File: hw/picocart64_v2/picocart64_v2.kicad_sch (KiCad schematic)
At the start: 0 parts

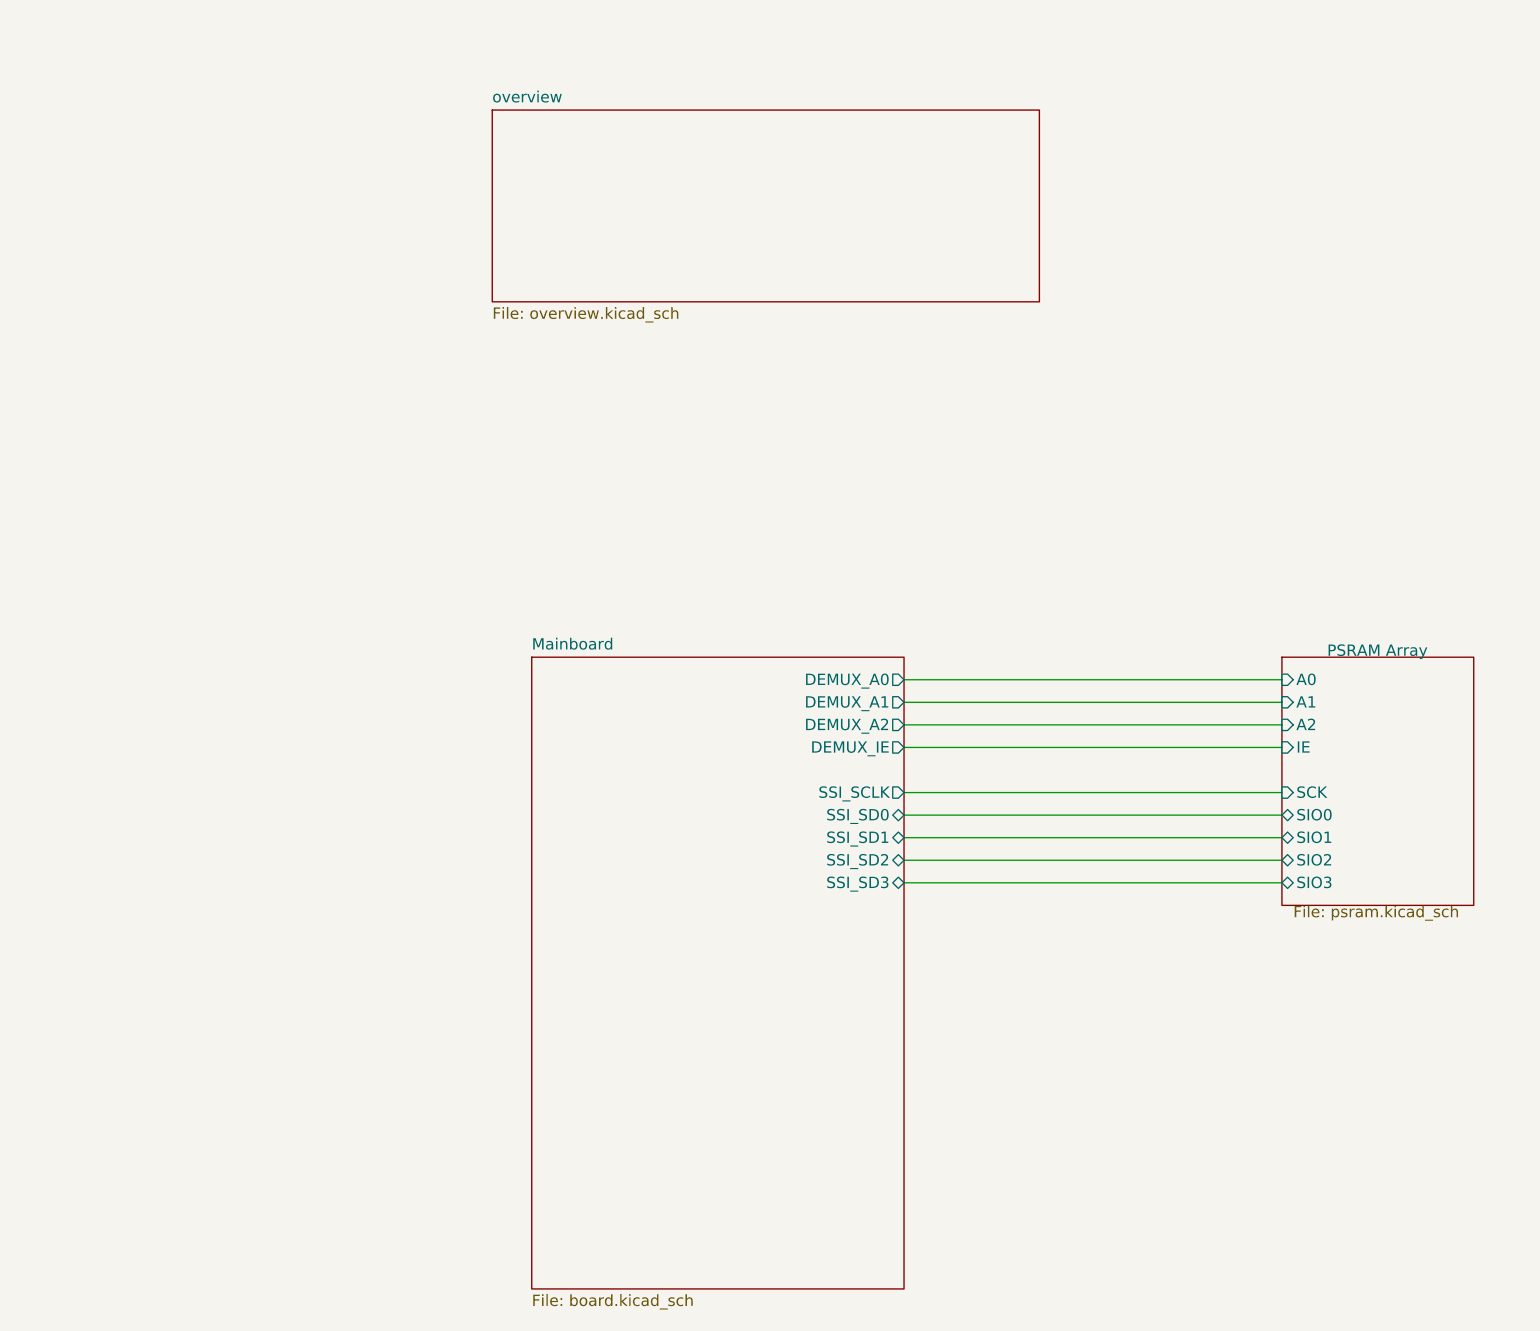
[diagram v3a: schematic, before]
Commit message: Documented and figured out some stuff
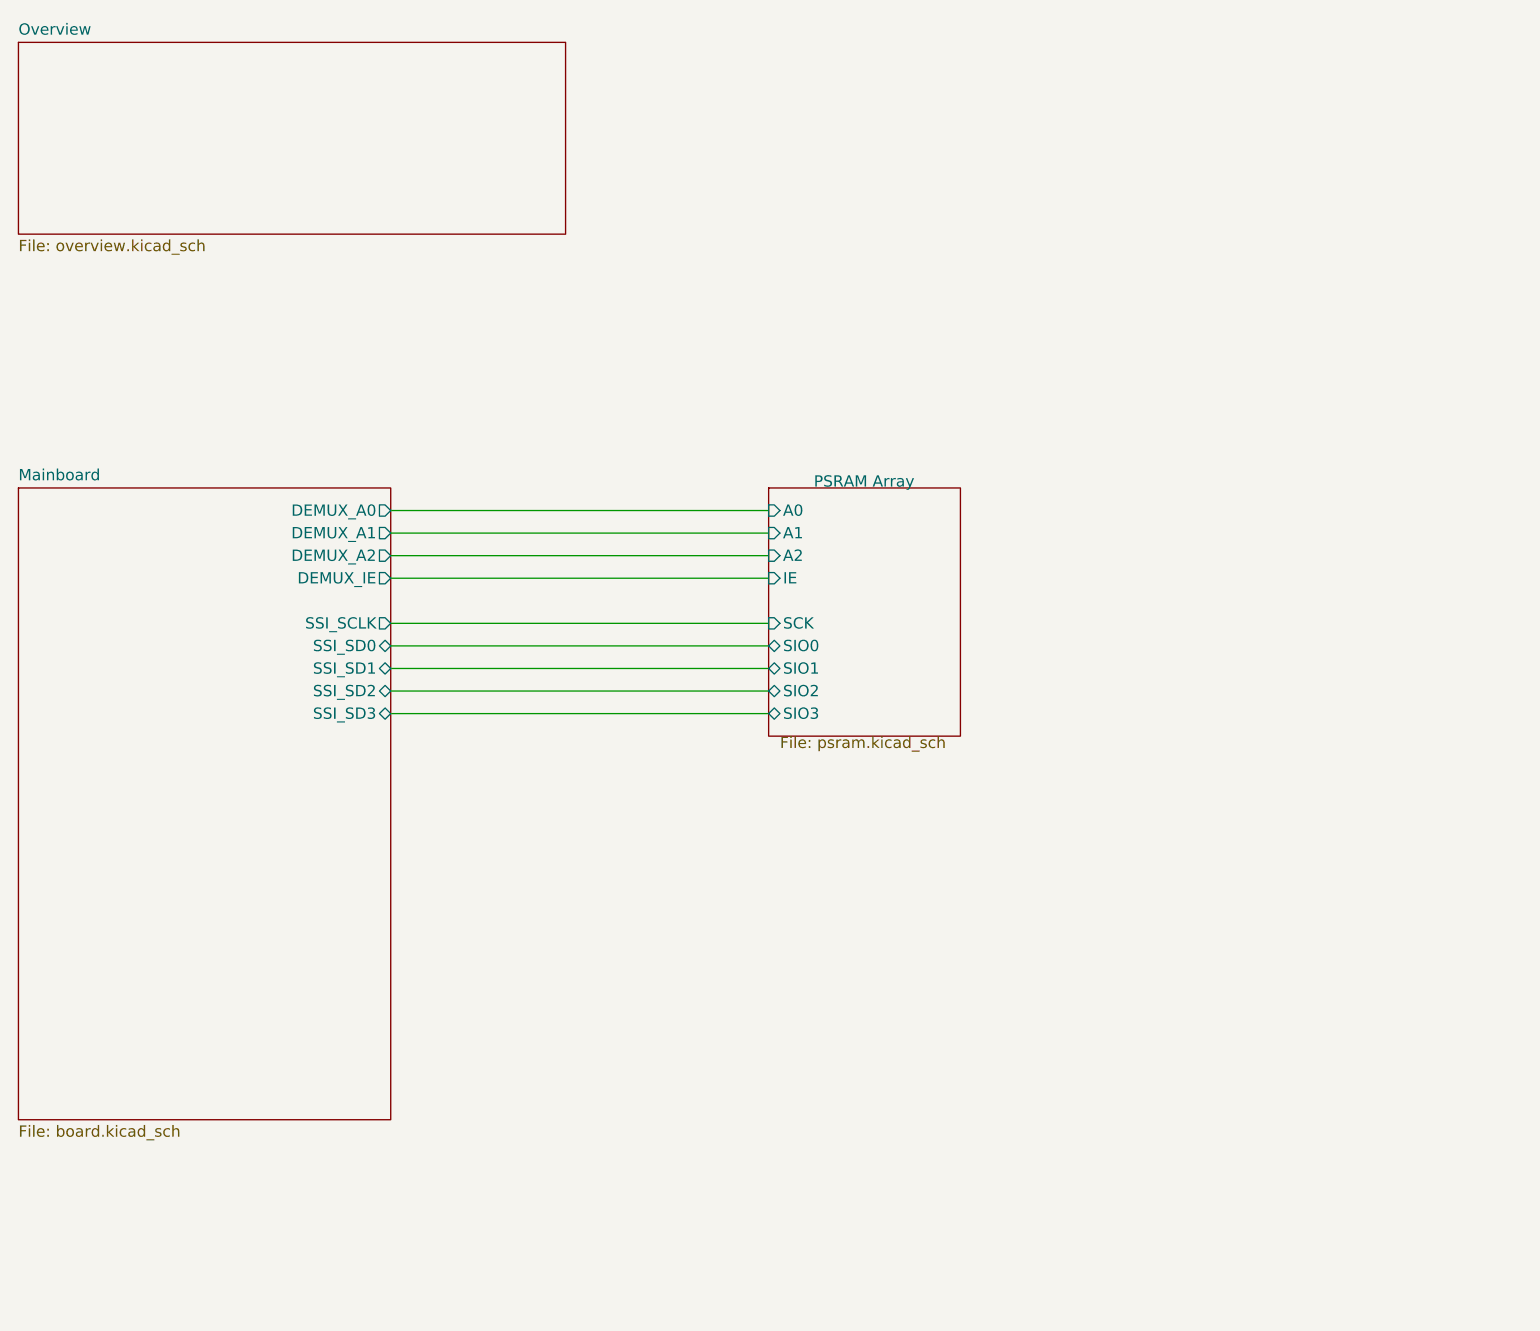
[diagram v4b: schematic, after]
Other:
- sheet overview renamed Overview
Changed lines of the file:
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@@
 (kicad_sch (version 20211123) (generator eeschema)
-  (paper "A3")
+  (paper "A4")
   (title_block
     (title "PicoCart64")
@@
     (company "Konrad Beckmann")
   )
-  (wire (pts (xy 158.115 105.41) (xy 200.66 105.41))
+  (wire (pts (xy 100.33 86.36) (xy 142.875 86.36))
     (stroke (width 0) (type default) (color 0 0 0 0))
   )
-  (wire (pts (xy 158.115 107.95) (xy 200.66 107.95))
+  (wire (pts (xy 100.33 88.9) (xy 142.875 88.9))
     (stroke (width 0) (type default) (color 0 0 0 0))
   )
-  (wire (pts (xy 158.115 110.49) (xy 200.66 110.49))
+  (wire (pts (xy 100.33 91.44) (xy 142.875 91.44))
     (stroke (width 0) (type default) (color 0 0 0 0))
   )
-  (wire (pts (xy 158.115 125.73) (xy 200.66 125.73))
+  (wire (pts (xy 100.33 106.68) (xy 142.875 106.68))
     (stroke (width 0) (type default) (color 0 0 0 0))
   )
-  (wire (pts (xy 158.115 115.57) (xy 200.66 115.57))
+  (wire (pts (xy 100.33 96.52) (xy 142.875 96.52))
     (stroke (width 0) (type default) (color 0 0 0 0))
   )
-  (wire (pts (xy 158.115 120.65) (xy 200.66 120.65))
+  (wire (pts (xy 100.33 101.6) (xy 142.875 101.6))
     (stroke (width 0) (type default) (color 0 0 0 0))
   )
-  (wire (pts (xy 158.115 123.19) (xy 200.66 123.19))
+  (wire (pts (xy 100.33 104.14) (xy 142.875 104.14))
     (stroke (width 0) (type default) (color 0 0 0 0))
   )
-  (wire (pts (xy 158.115 118.11) (xy 200.66 118.11))
+  (wire (pts (xy 100.33 99.06) (xy 142.875 99.06))
     (stroke (width 0) (type default) (color 0 0 0 0))
   )
-  (wire (pts (xy 158.115 102.87) (xy 200.66 102.87))
+  (wire (pts (xy 100.33 83.82) (xy 142.875 83.82))
     (stroke (width 0) (type default) (color 0 0 0 0))
   )
-  (sheet (at 200.66 100.33) (size 21.59 27.94)
+  (sheet (at 142.875 81.28) (size 21.59 27.94)
     (stroke (width 0.1524) (type solid) (color 0 0 0 0))
     (fill (color 255 221 221 1.0000))
-    (property "Sheet name" "PSRAM Array" (id 0) (at 205.74 100.33 0)
+    (property "Sheet name" "PSRAM Array" (id 0) (at 147.955 81.28 0)
       (effects (font (size 1.27 1.27)) (justify left bottom))
     )
-    (property "Sheet file" "psram.kicad_sch" (id 1) (at 201.93 128.27 0)
+    (property "Sheet file" "psram.kicad_sch" (id 1) (at 144.145 109.22 0)
       (effects (font (size 1.27 1.27)) (justify left top))
     )
-    (pin "A0" input (at 200.66 102.87 180)
+    (pin "A0" input (at 142.875 83.82 180)
       (effects (font (size 1.27 1.27)) (justify left))
     )
-    (pin "A1" input (at 200.66 105.41 180)
+    (pin "A1" input (at 142.875 86.36 180)
       (effects (font (size 1.27 1.27)) (justify left))
     )
-    (pin "A2" input (at 200.66 107.95 180)
+    (pin "A2" input (at 142.875 88.9 180)
       (effects (font (size 1.27 1.27)) (justify left))
     )
-    (pin "IE" input (at 200.66 110.49 180)
+    (pin "IE" input (at 142.875 91.44 180)
       (effects (font (size 1.27 1.27)) (justify left))
     )
-    (pin "SIO0" bidirectional (at 200.66 118.11 180)
+    (pin "SIO0" bidirectional (at 142.875 99.06 180)
       (effects (font (size 1.27 1.27)) (justify left))
     )
-    (pin "SIO1" bidirectional (at 200.66 120.65 180)
+    (pin "SIO1" bidirectional (at 142.875 101.6 180)
       (effects (font (size 1.27 1.27)) (justify left))
     )
-    (pin "SIO2" bidirectional (at 200.66 123.19 180)
+    (pin "SIO2" bidirectional (at 142.875 104.14 180)
       (effects (font (size 1.27 1.27)) (justify left))
     )
-    (pin "SIO3" bidirectional (at 200.66 125.73 180)
+    (pin "SIO3" bidirectional (at 142.875 106.68 180)
       (effects (font (size 1.27 1.27)) (justify left))
     )
-    (pin "SCK" input (at 200.66 115.57 180)
+    (pin "SCK" input (at 142.875 96.52 180)
       (effects (font (size 1.27 1.27)) (justify left))
     )
   )
-  (sheet (at 116.205 100.33) (size 41.91 71.12) (fields_autoplaced)
+  (sheet (at 58.42 81.28) (size 41.91 71.12) (fields_autoplaced)
     (stroke (width 0.1524) (type solid) (color 0 0 0 0))
     (fill (color 255 221 221 1.0000))
-    (property "Sheet name" "Mainboard" (id 0) (at 116.205 99.6184 0)
+    (property "Sheet name" "Mainboard" (id 0) (at 58.42 80.5684 0)
       (effects (font (size 1.27 1.27)) (justify left bottom))
     )
-    (property "Sheet file" "board.kicad_sch" (id 1) (at 116.205 172.0346 0)
+    (property "Sheet file" "board.kicad_sch" (id 1) (at 58.42 152.9846 0)
       (effects (font (size 1.27 1.27)) (justify left top))
     )
-    (pin "SSI_SD3" bidirectional (at 158.115 125.73 0)
+    (pin "SSI_SD3" bidirectional (at 100.33 106.68 0)
       (effects (font (size 1.27 1.27)) (justify right))
     )
-    (pin "SSI_SD2" bidirectional (at 158.115 123.19 0)
+    (pin "SSI_SD2" bidirectional (at 100.33 104.14 0)
       (effects (font (size 1.27 1.27)) (justify right))
     )
-    (pin "SSI_SD1" bidirectional (at 158.115 120.65 0)
+    (pin "SSI_SD1" bidirectional (at 100.33 101.6 0)
       (effects (font (size 1.27 1.27)) (justify right))
     )
-    (pin "DEMUX_A0" output (at 158.115 102.87 0)
+    (pin "DEMUX_A0" output (at 100.33 83.82 0)
       (effects (font (size 1.27 1.27)) (justify right))
     )
-    (pin "DEMUX_A2" output (at 158.115 107.95 0)
+    (pin "DEMUX_A2" output (at 100.33 88.9 0)
       (effects (font (size 1.27 1.27)) (justify right))
     )
-    (pin "DEMUX_A1" output (at 158.115 105.41 0)
+    (pin "DEMUX_A1" output (at 100.33 86.36 0)
       (effects (font (size 1.27 1.27)) (justify right))
     )
-    (pin "DEMUX_IE" output (at 158.115 110.49 0)
+    (pin "DEMUX_IE" output (at 100.33 91.44 0)
       (effects (font (size 1.27 1.27)) (justify right))
     )
-    (pin "SSI_SCLK" output (at 158.115 115.57 0)
+    (pin "SSI_SCLK" output (at 100.33 96.52 0)
       (effects (font (size 1.27 1.27)) (justify right))
     )
-    (pin "SSI_SD0" bidirectional (at 158.115 118.11 0)
+    (pin "SSI_SD0" bidirectional (at 100.33 99.06 0)
       (effects (font (size 1.27 1.27)) (justify right))
     )
   )
-  (sheet (at 111.76 38.735) (size 61.595 21.59) (fields_autoplaced)
+  (sheet (at 58.42 31.115) (size 61.595 21.59) (fields_autoplaced)
     (stroke (width 0.1524) (type solid) (color 0 0 0 0))
-    (fill (color 0 0 0 0.0000))
-    (property "Sheet name" "overview" (id 0) (at 111.76 38.0234 0)
+    (fill (color 155 255 155 1.0000))
+    (property "Sheet name" "Overview" (id 0) (at 58.42 30.4034 0)
       (effects (font (size 1.27 1.27)) (justify left bottom))
     )
-    (property "Sheet file" "overview.kicad_sch" (id 1) (at 111.76 60.9096 0)
+    (property "Sheet file" "overview.kicad_sch" (id 1) (at 58.42 53.2896 0)
       (effects (font (size 1.27 1.27)) (justify left top))
     )
